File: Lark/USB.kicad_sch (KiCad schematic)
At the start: 4 parts, among them J1 2169890002, U6 USBLC6-2SC6

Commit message: Update USB.kicad_sch
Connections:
- net D+: now also U6.4; no longer U6.6
- net D-: now also U6.6; no longer U6.4
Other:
- moved on the sheet: R24, R25, U6

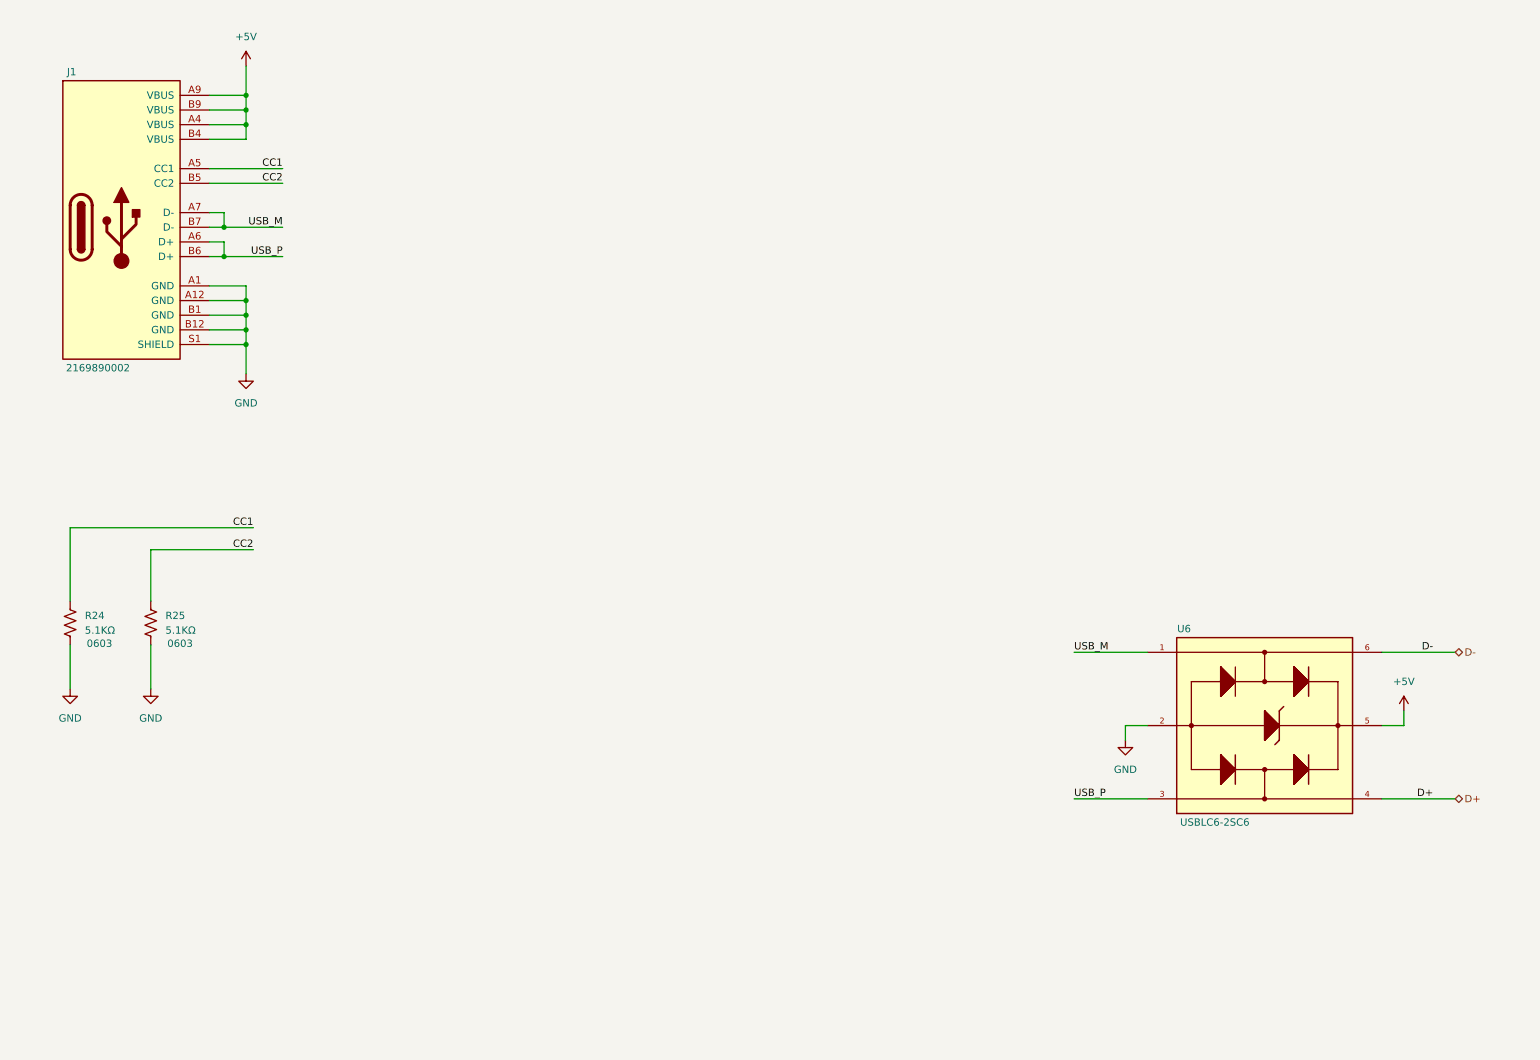
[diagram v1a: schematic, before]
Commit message: still porting design over from 'other' cad software.
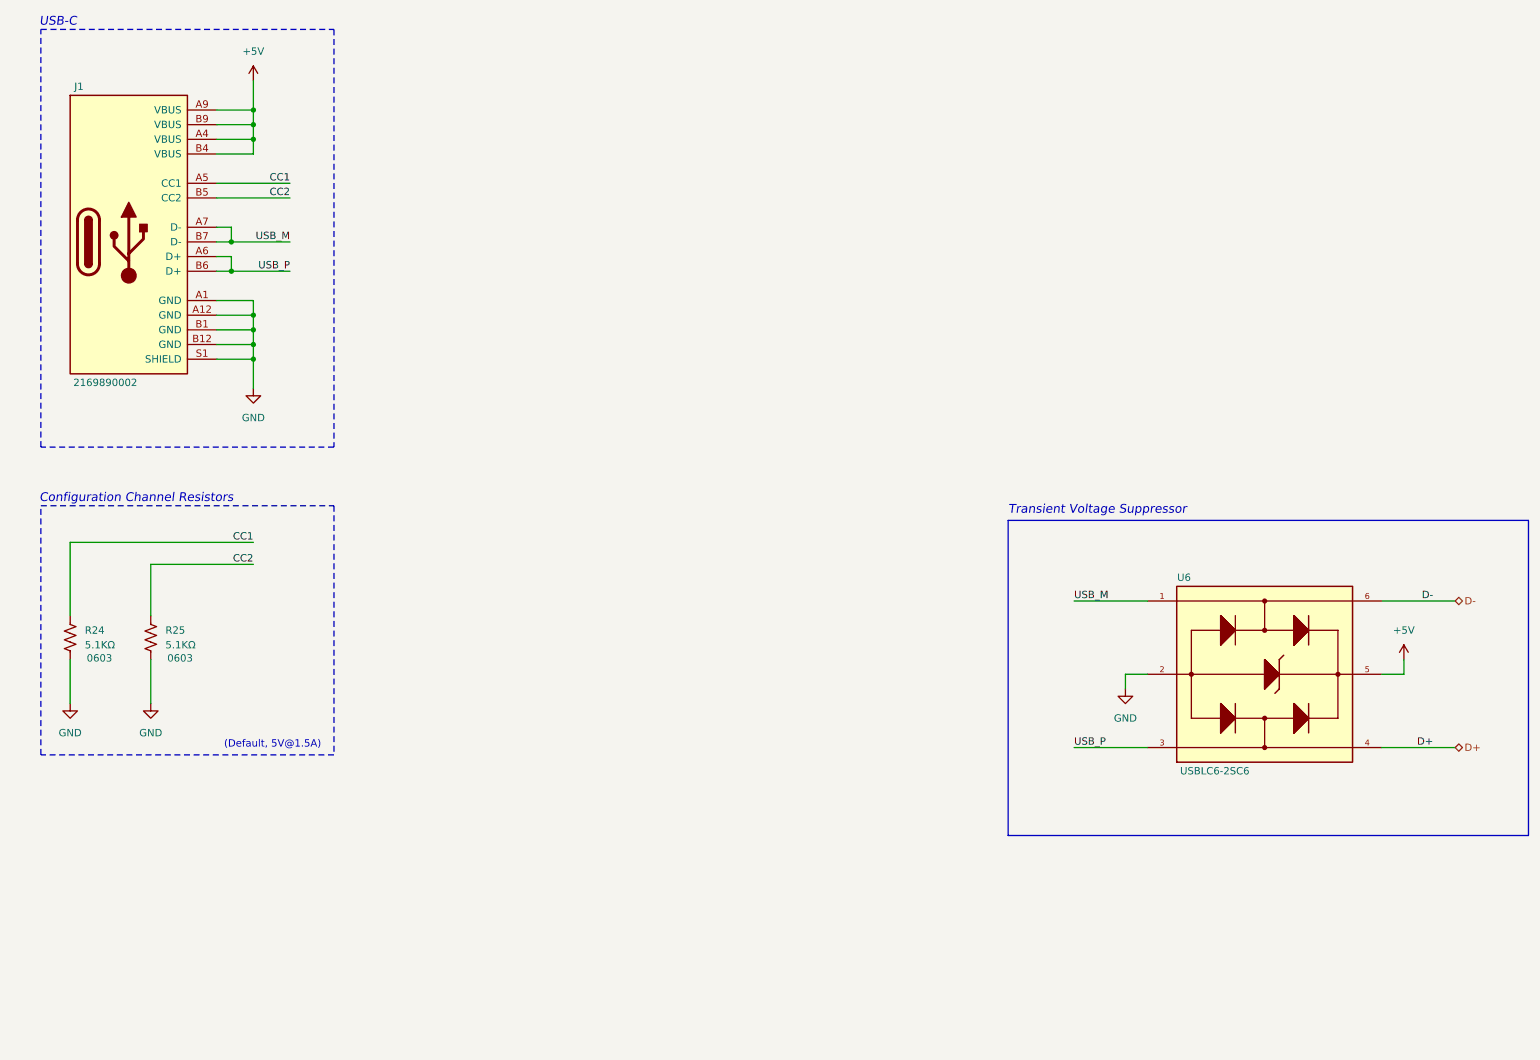
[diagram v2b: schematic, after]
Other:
- note added: "(Default, 5V@1.5A)"
- note added: "Configuration Channel Resistors"
- note added: "Transient Voltage Suppressor"
- note added: "USB-C"
- moved on the sheet: J1, R24, R25, U6

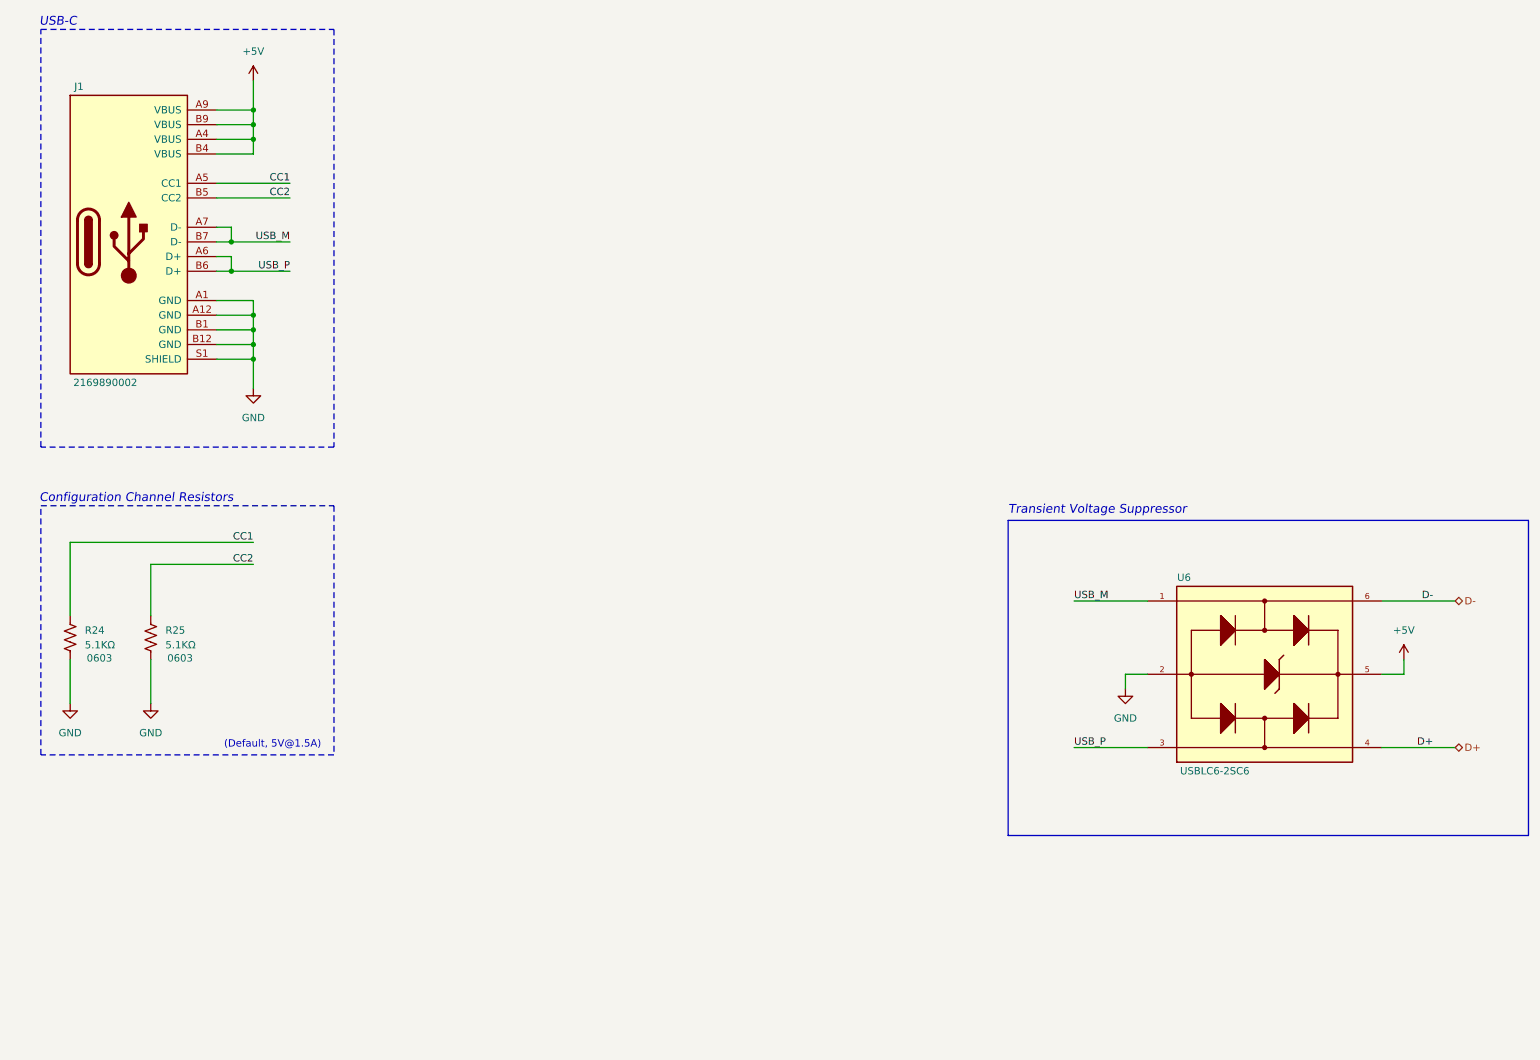
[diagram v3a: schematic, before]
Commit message: update, WIP
- Reannotated schematic.
- Added STM32 device.
- Fixed High-side switch (removed soft-start cap for device safety).
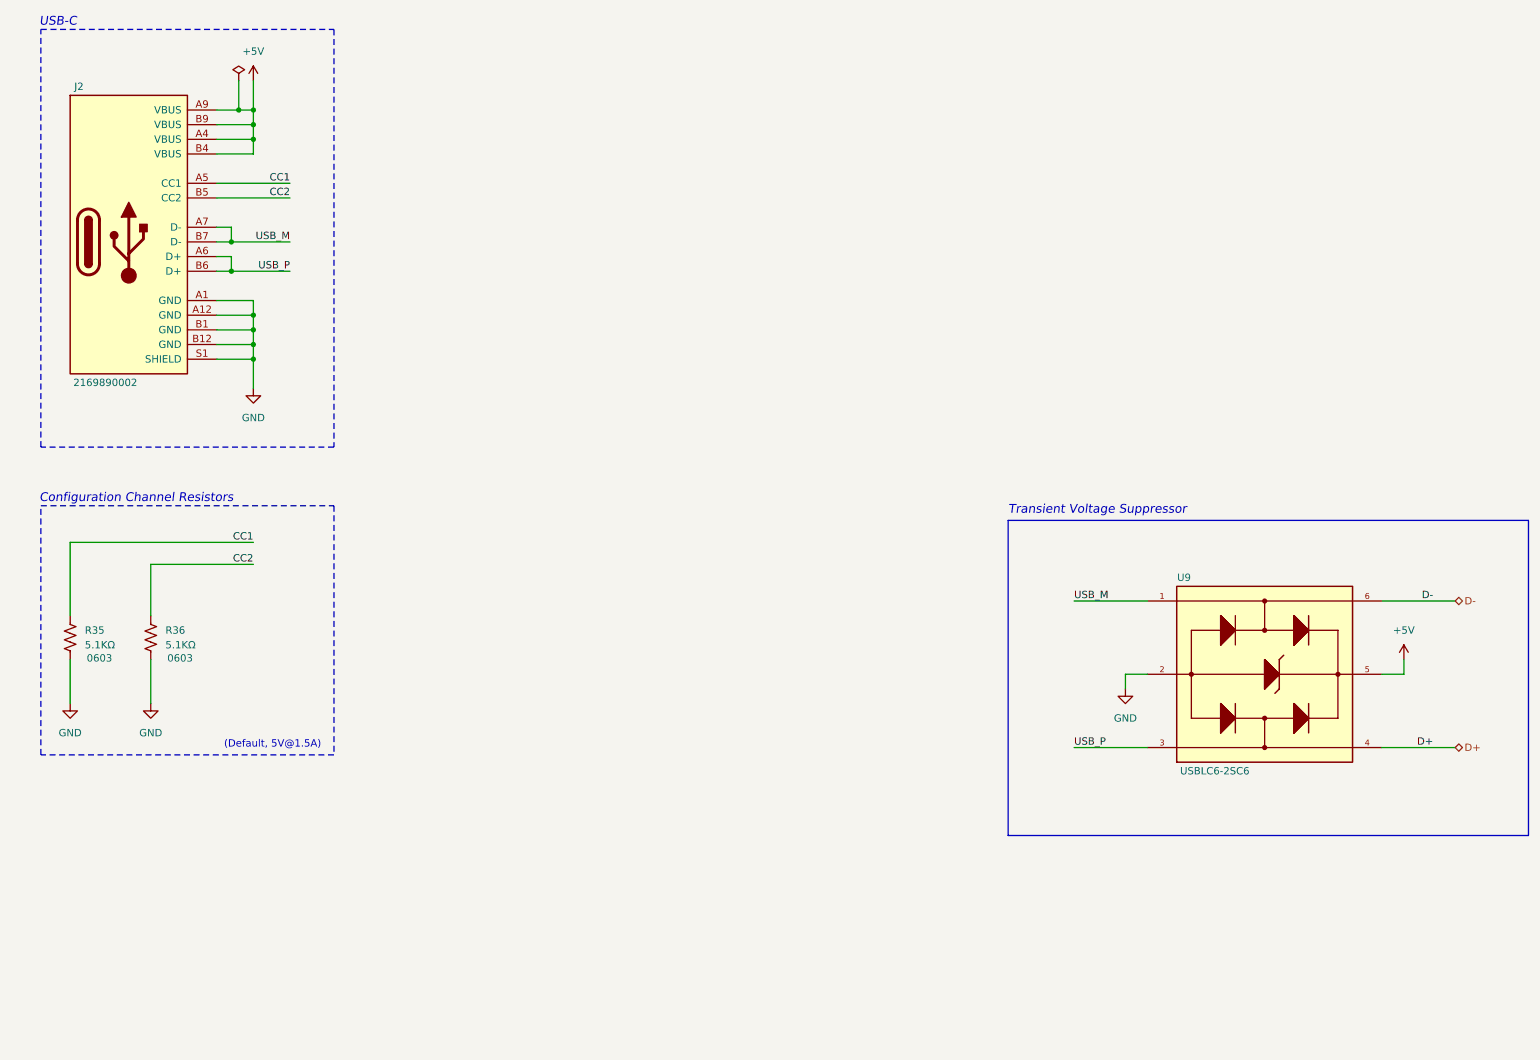
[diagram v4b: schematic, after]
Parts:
- renumbered J1 to J2, R24 to R35, R25 to R36, U6 to U9
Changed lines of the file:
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@@
+	)
+	(junction
+		(at 54.61 33.02)
+		(diameter 0)
+		(color 0 0 0 0)
 	)
 	(junction
@@
 	(wire
 		(pts
-			(xy 57.15 33.02) (xy 57.15 27.94)
-		)
-		(stroke
-			(width 0)
-			(type default)
-		)
-	)
-	(wire
-		(pts
 			(xy 53.34 58.42) (xy 53.34 60.96)
 		)
@@
 	(wire
 		(pts
+			(xy 50.8 33.02) (xy 54.61 33.02)
+		)
+		(stroke
+			(width 0)
+			(type default)
+		)
+	)
+	(wire
+		(pts
 			(xy 50.8 58.42) (xy 53.34 58.42)
 		)
@@
 	(wire
 		(pts
+			(xy 54.61 33.02) (xy 57.15 33.02)
+		)
+		(stroke
+			(width 0)
+			(type default)
+		)
+	)
+	(wire
+		(pts
 			(xy 57.15 68.58) (xy 57.15 71.12)
 		)
@@
 	(wire
 		(pts
-			(xy 50.8 33.02) (xy 57.15 33.02)
-		)
-		(stroke
-			(width 0)
-			(type default)
-		)
-	)
-	(wire
-		(pts
 			(xy 50.8 55.88) (xy 53.34 55.88)
 		)
@@
 	(wire
 		(pts
+			(xy 54.61 27.94) (xy 54.61 33.02)
+		)
+		(stroke
+			(width 0)
+			(type default)
+		)
+	)
+	(wire
+		(pts
 			(xy 57.15 73.66) (xy 57.15 76.2)
 		)
@@
 		(pts
 			(xy 57.15 66.04) (xy 57.15 68.58)
+		)
+		(stroke
+			(width 0)
+			(type default)
+		)
+	)
+	(wire
+		(pts
+			(xy 57.15 27.94) (xy 57.15 33.02)
 		)
 		(stroke
@@
 		(dnp no)
 		(fields_autoplaced yes)
-		(property "Reference" "#PWR051"
+		(property "Reference" "#PWR093"
 			(at 57.15 87.63 0)
 			(effects
@@
 			(project ""
 				(path "/a351af57-4353-47da-9f45-7393de572768/9aa817d4-eb96-4675-9e22-be0e45d55bef"
-					(reference "#PWR051")
+					(reference "#PWR093")
 					(unit 1)
 				)
@@
 		(dnp no)
 		(fields_autoplaced yes)
-		(property "Reference" "#PWR050"
+		(property "Reference" "#PWR092"
 			(at 57.15 31.75 0)
 			(effects
@@
 			(project ""
 				(path "/a351af57-4353-47da-9f45-7393de572768/9aa817d4-eb96-4675-9e22-be0e45d55bef"
-					(reference "#PWR050")
+					(reference "#PWR092")
 					(unit 1)
 				)
@@
 		(on_board yes)
 		(dnp no)
-		(property "Reference" "J1"
+		(property "Reference" "J2"
 			(at 26.924 28.956 0)
 			(effects
@@
 			(project ""
 				(path "/a351af57-4353-47da-9f45-7393de572768/9aa817d4-eb96-4675-9e22-be0e45d55bef"
-					(reference "J1")
+					(reference "J2")
 					(unit 1)
 				)
@@
 		(dnp no)
 		(fields_autoplaced yes)
-		(property "Reference" "#PWR053"
+		(property "Reference" "#PWR094"
 			(at 256.54 132.08 0)
 			(effects
@@
 			(project "Lark"
 				(path "/a351af57-4353-47da-9f45-7393de572768/9aa817d4-eb96-4675-9e22-be0e45d55bef"
-					(reference "#PWR053")
+					(reference "#PWR094")
 					(unit 1)
 				)
@@
 		(on_board yes)
 		(dnp no)
-		(property "Reference" "R25"
+		(property "Reference" "R36"
 			(at 41.91 123.1899 0)
 			(effects
@@
 			(project "Lark"
 				(path "/a351af57-4353-47da-9f45-7393de572768/9aa817d4-eb96-4675-9e22-be0e45d55bef"
-					(reference "R25")
+					(reference "R36")
 					(unit 1)
 				)
@@
 		(on_board yes)
 		(dnp no)
-		(property "Reference" "R24"
+		(property "Reference" "R35"
 			(at 27.94 123.1899 0)
 			(effects
@@
 			(project "Lark"
 				(path "/a351af57-4353-47da-9f45-7393de572768/9aa817d4-eb96-4675-9e22-be0e45d55bef"
-					(reference "R24")
+					(reference "R35")
 					(unit 1)
 				)
@@
 		(on_board yes)
 		(dnp no)
-		(property "Reference" "U6"
+		(property "Reference" "U9"
 			(at 218.44 114.046 0)
 			(effects
@@
 			(project ""
 				(path "/a351af57-4353-47da-9f45-7393de572768/9aa817d4-eb96-4675-9e22-be0e45d55bef"
-					(reference "U6")
+					(reference "U9")
+					(unit 1)
+				)
+			)
+		)
+	)
+	(symbol
+		(lib_id "power:PWR_FLAG")
+		(at 54.61 27.94 0)
+		(unit 1)
+		(exclude_from_sim no)
+		(in_bom yes)
+		(on_board yes)
+		(dnp no)
+		(fields_autoplaced yes)
+		(property "Reference" "#FLG05"
+			(at 54.61 26.035 0)
+			(effects
+				(font
+					(size 1.27 1.27)
+				)
+				(hide yes)
+			)
+		)
+		(property "Value" "PWR_FLAG"
+			(at 54.61 22.86 0)
+			(effects
+				(font
+					(size 1.27 1.27)
+				)
+				(hide yes)
+			)
+		)
+		(property "Footprint" ""
+			(at 54.61 27.94 0)
+			(effects
+				(font
+					(size 1.27 1.27)
+				)
+				(hide yes)
+			)
+		)
+		(property "Datasheet" "~"
+			(at 54.61 27.94 0)
+			(effects
+				(font
+					(size 1.27 1.27)
+				)
+				(hide yes)
+			)
+		)
+		(property "Description" "Special symbol for telling ERC where power comes from"
+			(at 54.61 27.94 0)
+			(effects
+				(font
+					(size 1.27 1.27)
+				)
+				(hide yes)
+			)
+		)
+		(pin "1"
+		)
+		(instances
+			(project ""
+				(path "/a351af57-4353-47da-9f45-7393de572768/9aa817d4-eb96-4675-9e22-be0e45d55bef"
+					(reference "#FLG05")
 					(unit 1)
 				)
@@
 		(dnp no)
 		(fields_autoplaced yes)
-		(property "Reference" "#PWR052"
+		(property "Reference" "#PWR095"
 			(at 208.28 139.7 0)
 			(effects
@@
 			(project "Lark"
 				(path "/a351af57-4353-47da-9f45-7393de572768/9aa817d4-eb96-4675-9e22-be0e45d55bef"
-					(reference "#PWR052")
+					(reference "#PWR095")
 					(unit 1)
 				)
@@
 		(dnp no)
 		(fields_autoplaced yes)
-		(property "Reference" "#PWR054"
+		(property "Reference" "#PWR096"
 			(at 25.4 142.24 0)
 			(effects
@@
 			(project "Lark"
 				(path "/a351af57-4353-47da-9f45-7393de572768/9aa817d4-eb96-4675-9e22-be0e45d55bef"
-					(reference "#PWR054")
+					(reference "#PWR096")
 					(unit 1)
 				)
@@
 		(dnp no)
 		(fields_autoplaced yes)
-		(property "Reference" "#PWR055"
+		(property "Reference" "#PWR097"
 			(at 39.37 142.24 0)
 			(effects
@@
 			(project "Lark"
 				(path "/a351af57-4353-47da-9f45-7393de572768/9aa817d4-eb96-4675-9e22-be0e45d55bef"
-					(reference "#PWR055")
+					(reference "#PWR097")
 					(unit 1)
 				)

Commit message: Updated schematic, WIP
- Added NOR flash part.
- Added new CubeMX config file.
- Reannotated the schematic.
- Made some more connections to the MCU.
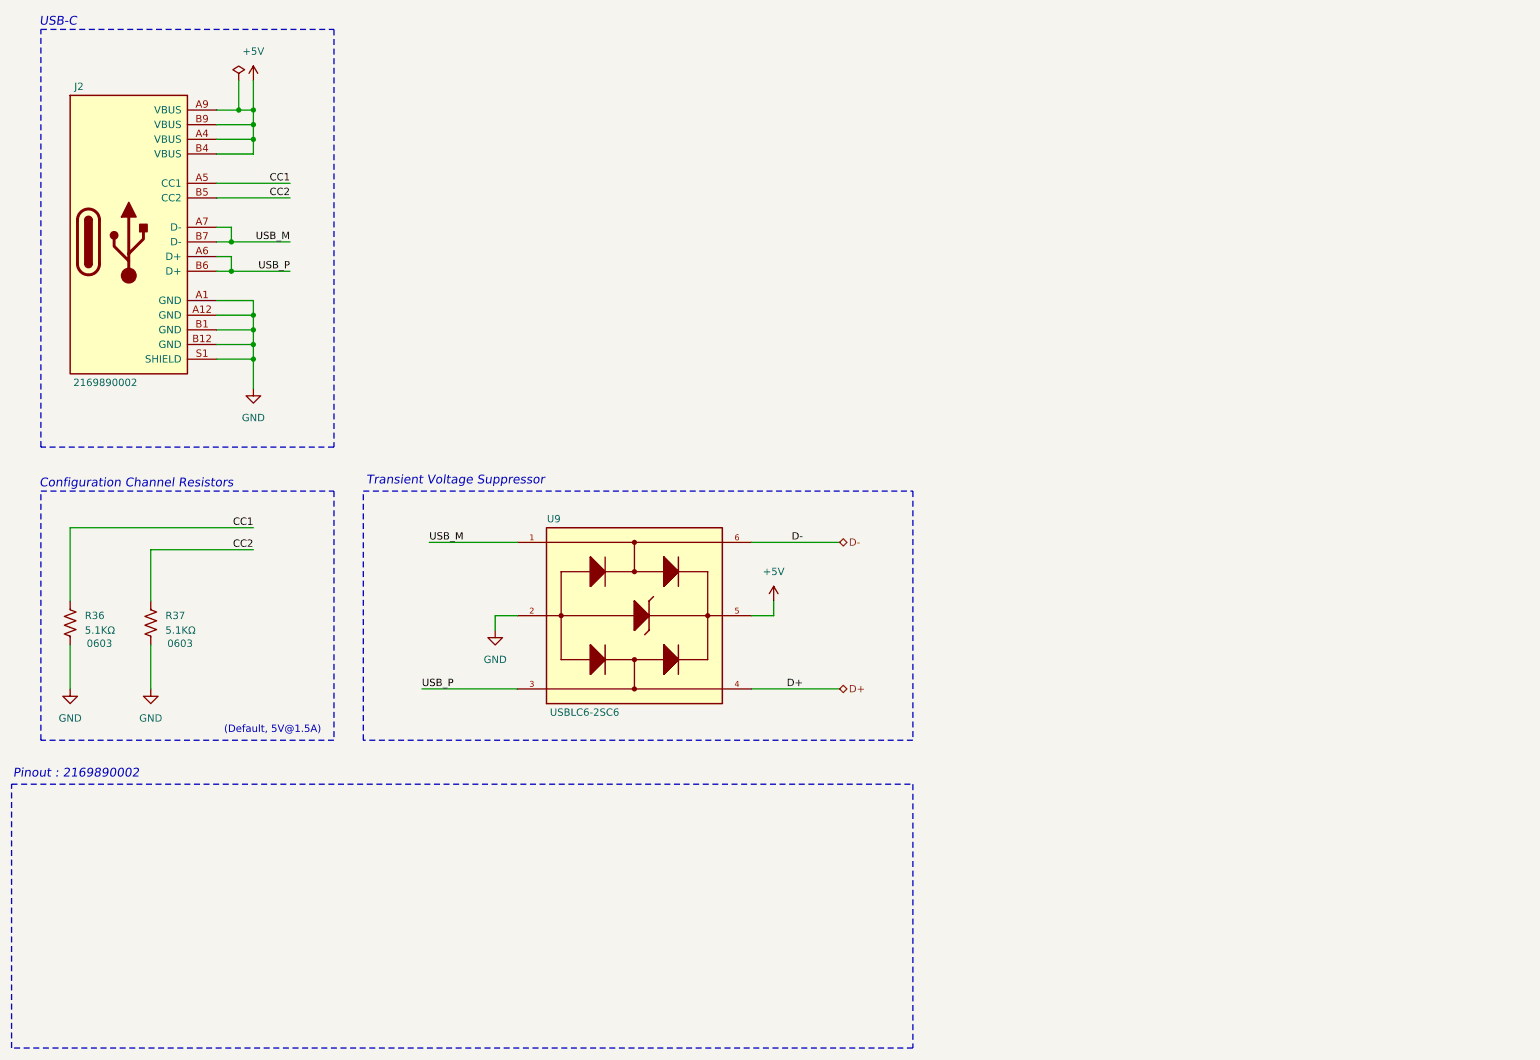
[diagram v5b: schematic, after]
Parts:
- renumbered R35 to R36, R36 to R37
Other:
- note added: "Pinout : 2169890002"
- moved on the sheet: R36, R37, U9
